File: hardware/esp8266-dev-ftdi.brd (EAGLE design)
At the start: 50 x 50 mm, 55 parts, among them CON1 USBMICRO-NO_CENTER-LONG_PADS

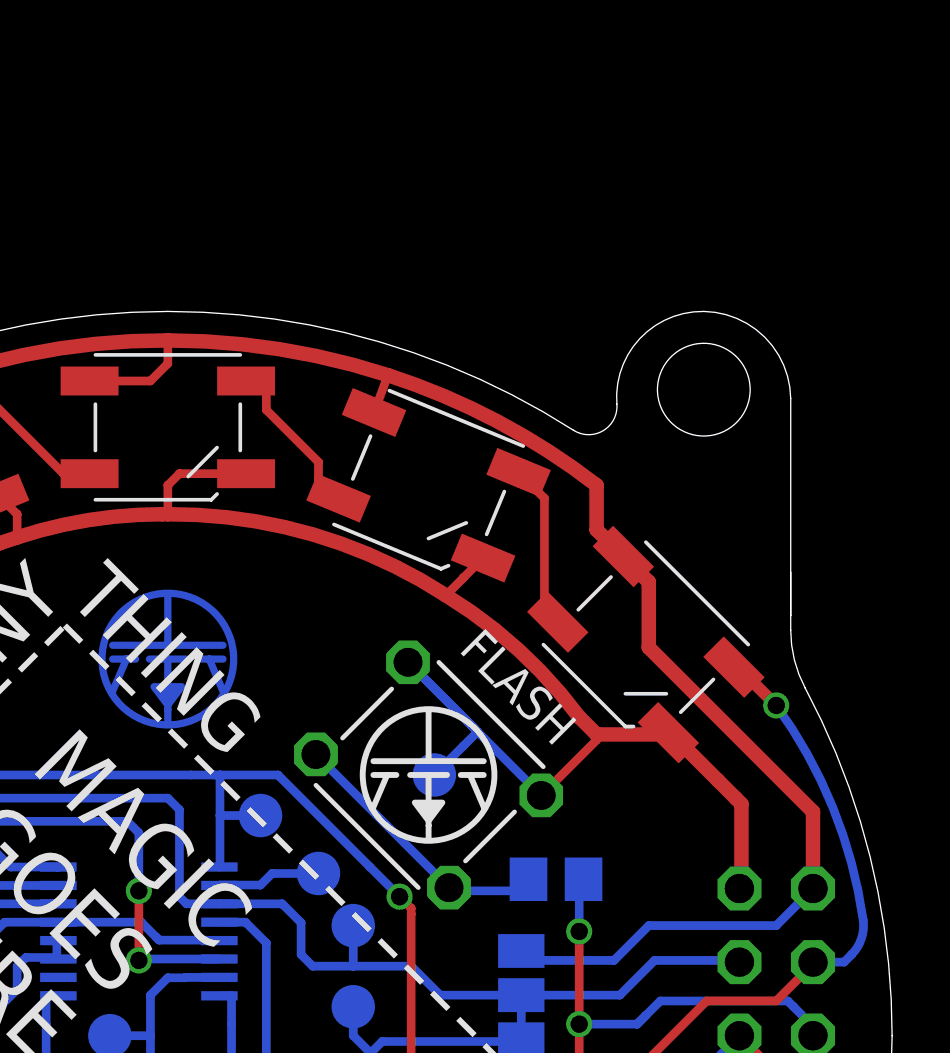
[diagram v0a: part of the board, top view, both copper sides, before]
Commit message: added led to gpio2
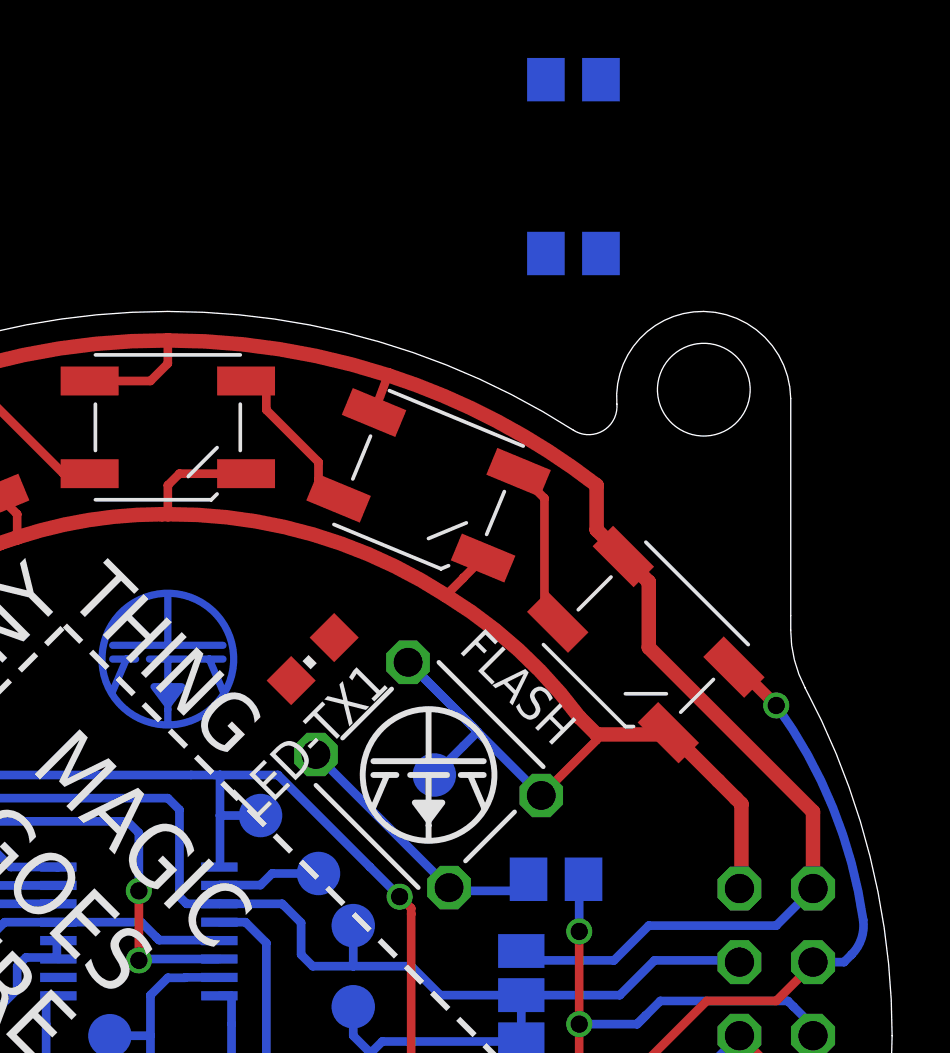
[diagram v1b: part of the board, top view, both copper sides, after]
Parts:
- added LED-TX1: (no value), p.peter-leds:CHIPLED_0805
- added R12, R13: 10k, p.peter-rcl:R0805
- R7: value 10k -> 2k
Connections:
- new net N$22: LED-TX1.A, R13.1
- net +3V3: now also R12.2
- net GND: now also LED-TX1.C
- net IO0: now also R12.1, R13.2
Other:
- outline, holes or cut-outs redrawn
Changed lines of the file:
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@@
 <?xml version="1.0" encoding="utf-8"?>
 <!DOCTYPE eagle SYSTEM "eagle.dtd">
-<eagle version="7.3.0">
+<eagle version="7.1.0">
 <drawing>
 <settings>
@@
 <grid distance="0.5" unitdist="mm" unit="mm" style="lines" multiple="1" display="yes" altdistance="0.1" altunitdist="mm" altunit="mm"/>
 <layers>
-<layer number="1" name="Top" color="4" fill="1" visible="no" active="yes"/>
+<layer number="1" name="Top" color="4" fill="1" visible="yes" active="yes"/>
 <layer number="16" name="Bottom" color="1" fill="1" visible="no" active="yes"/>
 <layer number="17" name="Pads" color="2" fill="1" visible="yes" active="yes"/>
 <layer number="18" name="Vias" color="2" fill="1" visible="yes" active="yes"/>
-<layer number="19" name="Unrouted" color="6" fill="1" visible="no" active="yes"/>
+<layer number="19" name="Unrouted" color="6" fill="1" visible="yes" active="yes"/>
 <layer number="20" name="Dimension" color="15" fill="1" visible="yes" active="yes"/>
 <layer number="21" name="tPlace" color="7" fill="1" visible="yes" active="yes"/>
@@
 <layer number="23" name="tOrigins" color="15" fill="1" visible="yes" active="yes"/>
 <layer number="24" name="bOrigins" color="15" fill="1" visible="no" active="yes"/>
-<layer number="25" name="tNames" color="7" fill="1" visible="yes" active="yes"/>
+<layer number="25" name="tNames" color="7" fill="1" visible="no" active="yes"/>
 <layer number="26" name="bNames" color="7" fill="1" visible="no" active="yes"/>
-<layer number="27" name="tValues" color="7" fill="1" visible="yes" active="yes"/>
+<layer number="27" name="tValues" color="7" fill="1" visible="no" active="yes"/>
 <layer number="28" name="bValues" color="7" fill="1" visible="no" active="yes"/>
 <layer number="29" name="tStop" color="7" fill="3" visible="yes" active="yes"/>
@@
 <layer number="39" name="tKeepout" color="4" fill="11" visible="yes" active="yes"/>
 <layer number="40" name="bKeepout" color="1" fill="11" visible="no" active="yes"/>
-<layer number="41" name="tRestrict" color="4" fill="10" visible="yes" active="yes"/>
+<layer number="41" name="tRestrict" color="4" fill="10" visible="no" active="yes"/>
 <layer number="42" name="bRestrict" color="1" fill="10" visible="no" active="yes"/>
 <layer number="43" name="vRestrict" color="2" fill="10" visible="no" active="yes"/>
 <layer number="44" name="Drills" color="7" fill="1" visible="no" active="yes"/>
-<layer number="45" name="Holes" color="7" fill="1" visible="no" active="yes"/>
+<layer number="45" name="Holes" color="7" fill="1" visible="yes" active="yes"/>
 <layer number="46" name="Milling" color="3" fill="1" visible="no" active="yes"/>
-<layer number="47" name="Measures" color="7" fill="1" visible="no" active="yes"/>
+<layer number="47" name="Measures" color="7" fill="1" visible="yes" active="yes"/>
 <layer number="48" name="Document" color="7" fill="1" visible="no" active="yes"/>
 <layer number="49" name="Reference" color="7" fill="1" visible="no" active="yes"/>
@@
 <layer number="110" name="fp0" color="7" fill="1" visible="no" active="yes"/>
 <layer number="116" name="Patch_BOT" color="9" fill="4" visible="no" active="yes"/>
-<layer number="121" name="_tsilk" color="7" fill="1" visible="yes" active="yes"/>
+<layer number="121" name="_tsilk" color="7" fill="1" visible="no" active="yes"/>
 <layer number="122" name="_bsilk" color="7" fill="1" visible="no" active="yes"/>
 <layer number="123" name="tTestmark" color="7" fill="1" visible="no" active="yes"/>
@@
 <wire x1="40.5" y1="46.8" x2="43.5" y2="50" width="0" layer="20" curve="-95.451873"/>
 <wire x1="43.5" y1="50" x2="46.5" y2="47" width="0" layer="20" curve="-88.245118"/>
-<wire x1="46.5" y1="41" x2="46.5" y2="39.5" width="0" layer="20"/>
 <wire x1="46.5" y1="39.5" x2="46.5" y2="39" width="0" layer="20"/>
 <wire x1="46.5" y1="47" x2="46.5" y2="39.5" width="0" layer="20"/>
@@
 <attribute name="VALUE" x="31.6" y="13.6" size="1.2" layer="28" font="vector" ratio="15" rot="MR270" align="center"/>
 </element>
-<element name="R7" library="p.peter-rcl" package="R0805" value="10k" x="38.4" y="30.4" smashed="yes" rot="MR0">
+<element name="R7" library="p.peter-rcl" package="R0805" value="2k" x="38.4" y="30.4" smashed="yes" rot="MR0">
 <attribute name="VALUE" x="40" y="32.2" size="1.2" layer="28" font="vector" ratio="15" rot="MR0" align="center"/>
 </element>
@@
 <attribute name="TP_SIGNAL_NAME" value="" x="34.2" y="31.46" size="1" layer="38" rot="MR0"/>
 </element>
+<element name="R12" library="p.peter-rcl" package="R0805" value="10k" x="39" y="58" rot="MR0"/>
+<element name="R13" library="p.peter-rcl" package="R0805" value="10k" x="39" y="52" rot="MR0"/>
+<element name="LED-TX1" library="p.peter-leds" package="CHIPLED_0805" value="" x="30" y="38" rot="R135"/>
 </elements>
 <signals>
@@
 <wire x1="34.2" y1="34" x2="35.2" y2="35" width="0.3" layer="16"/>
 <wire x1="35.2" y1="35" x2="35.6909875" y2="35.4909875" width="0.3" layer="16"/>
+<contactref element="LED-TX1" pad="C"/>
 <wire x1="15.294075" y1="20.694075" x2="15.305921875" y2="20.694075" width="0" layer="19" extent="16-16"/>
+<wire x1="29.2575375" y1="37.2575375" x2="9.8" y2="11.15" width="0" layer="19" extent="1-16"/>
 </signal>
 <signal name="+5V">
@@
 <wire x1="31.4" y1="26" x2="31.4" y2="25" width="0.3" layer="16"/>
 <wire x1="31.4" y1="25" x2="32" y2="24.4" width="0.3" layer="16"/>
+<contactref element="R12" pad="2"/>
+<wire x1="38.05" y1="58" x2="17" y2="3.4" width="0" layer="19" extent="1-16"/>
 </signal>
 <signal name="N$9">
@@
 <wire x1="39.2" y1="28.6" x2="39.2" y2="29.85" width="0.3" layer="16"/>
 <wire x1="39.2" y1="29.85" x2="39.35" y2="30.4" width="0.3" layer="16"/>
+<contactref element="R12" pad="1"/>
+<contactref element="R13" pad="2"/>
+<wire x1="39.95" y1="58" x2="31.7" y2="20.09605" width="0" layer="19" extent="1-1"/>
+<wire x1="38.05" y1="52" x2="39.95" y2="58" width="0" layer="19" extent="1-1"/>
 </signal>
 <signal name="N$1">
@@
 <wire x1="4.6" y1="18.59" x2="4.6" y2="18.65" width="0.3" layer="16"/>
 </signal>
+<signal name="N$22">
+<contactref element="R13" pad="1"/>
+<contactref element="LED-TX1" pad="A"/>
+<wire x1="39.95" y1="52" x2="30.742459375" y2="38.742459375" width="0" layer="19" extent="1-1"/>
+</signal>
 </signals>
